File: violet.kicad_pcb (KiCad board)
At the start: 2 copper layers, 190 x 204 mm, 47 parts, among them J1 NEIGHBOR1, J10 Conn_01x08, J2 NEIGHBOR2, J3 NEIGHBOR1, J4 BONUS_ROW, J5 NEIGHBOR2, J6 NEIGHBOR1, J7 BONUS_ROW, J8 BONUS_ROW, J9 NEIGHBOR2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

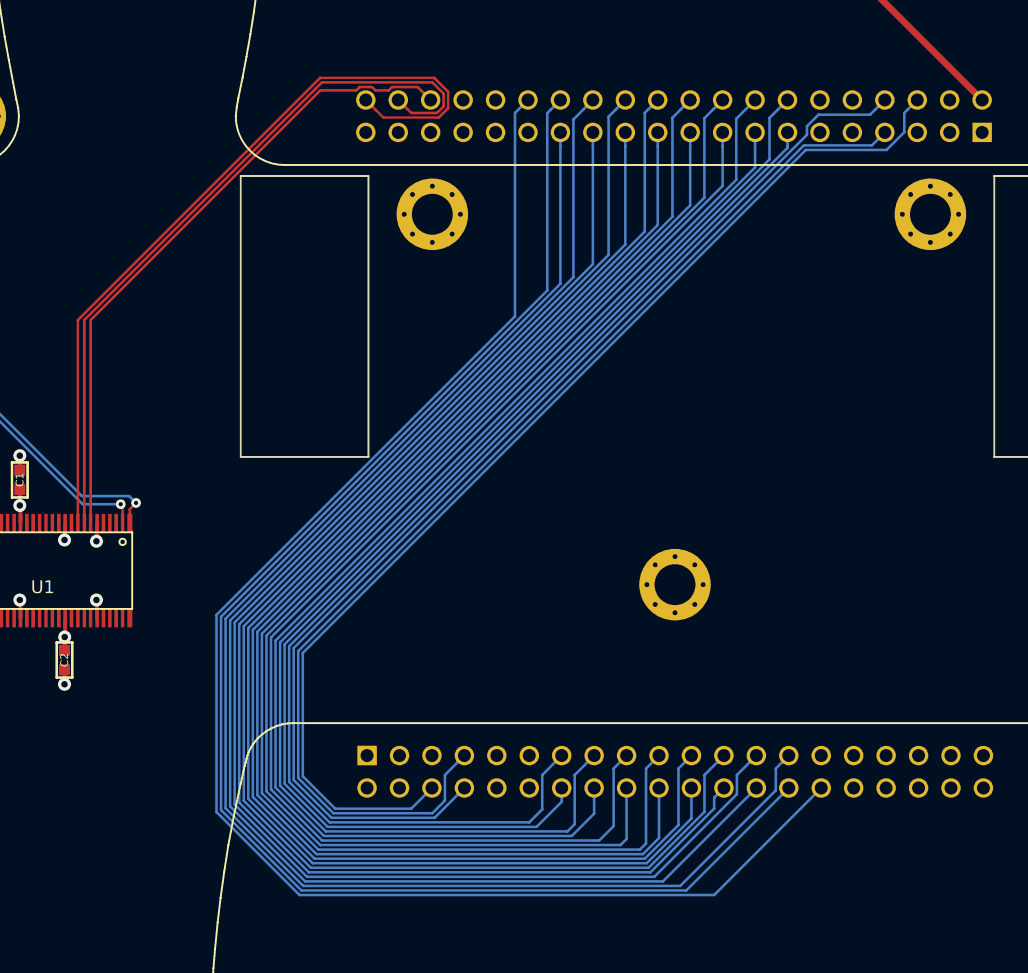
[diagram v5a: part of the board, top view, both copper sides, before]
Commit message: Re-map I/O expanders for easier routing
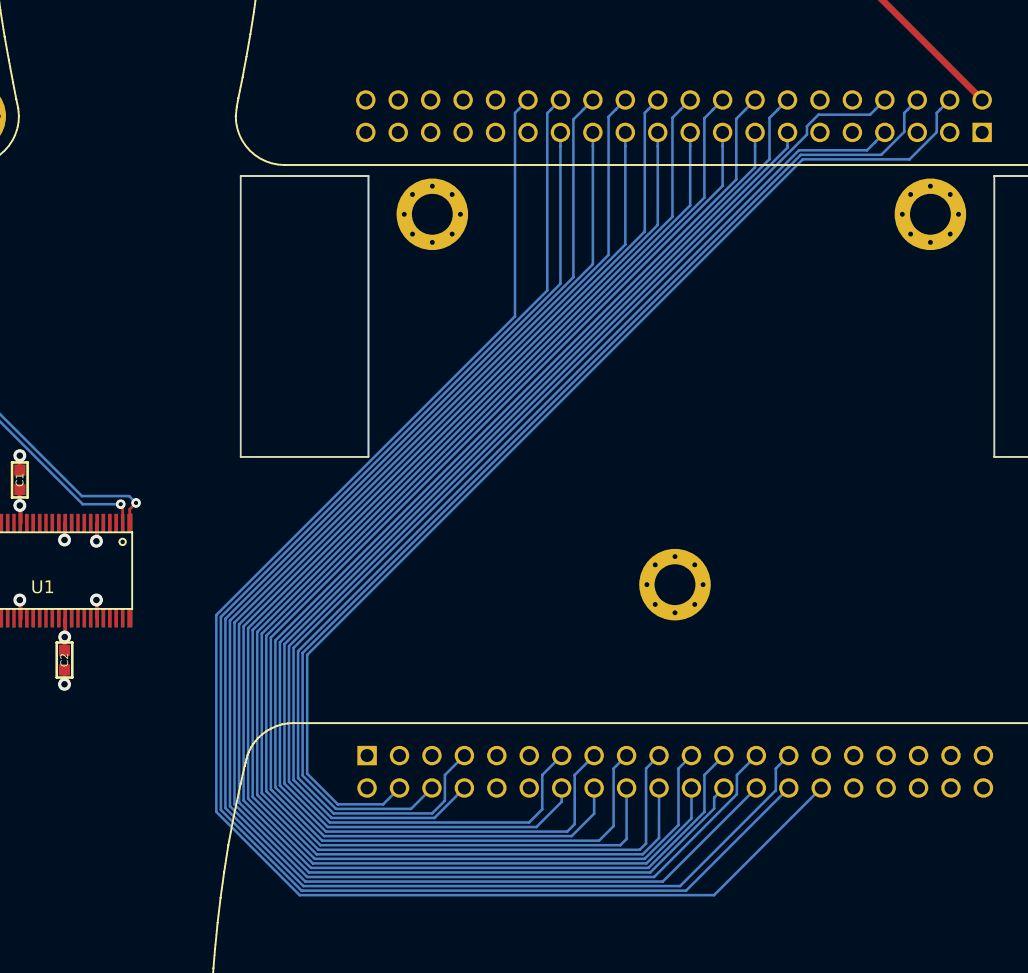
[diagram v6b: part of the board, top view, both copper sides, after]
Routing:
- net /EUT_P0_0: track 0.00 -> 87.2 mm
- net /U1_IO0_5: track 61.8 -> 0.00 mm
- net /U1_IO0_4: track 57.2 -> 0.00 mm
- net /U1_IO0_3: track 50.7 -> 0.00 mm

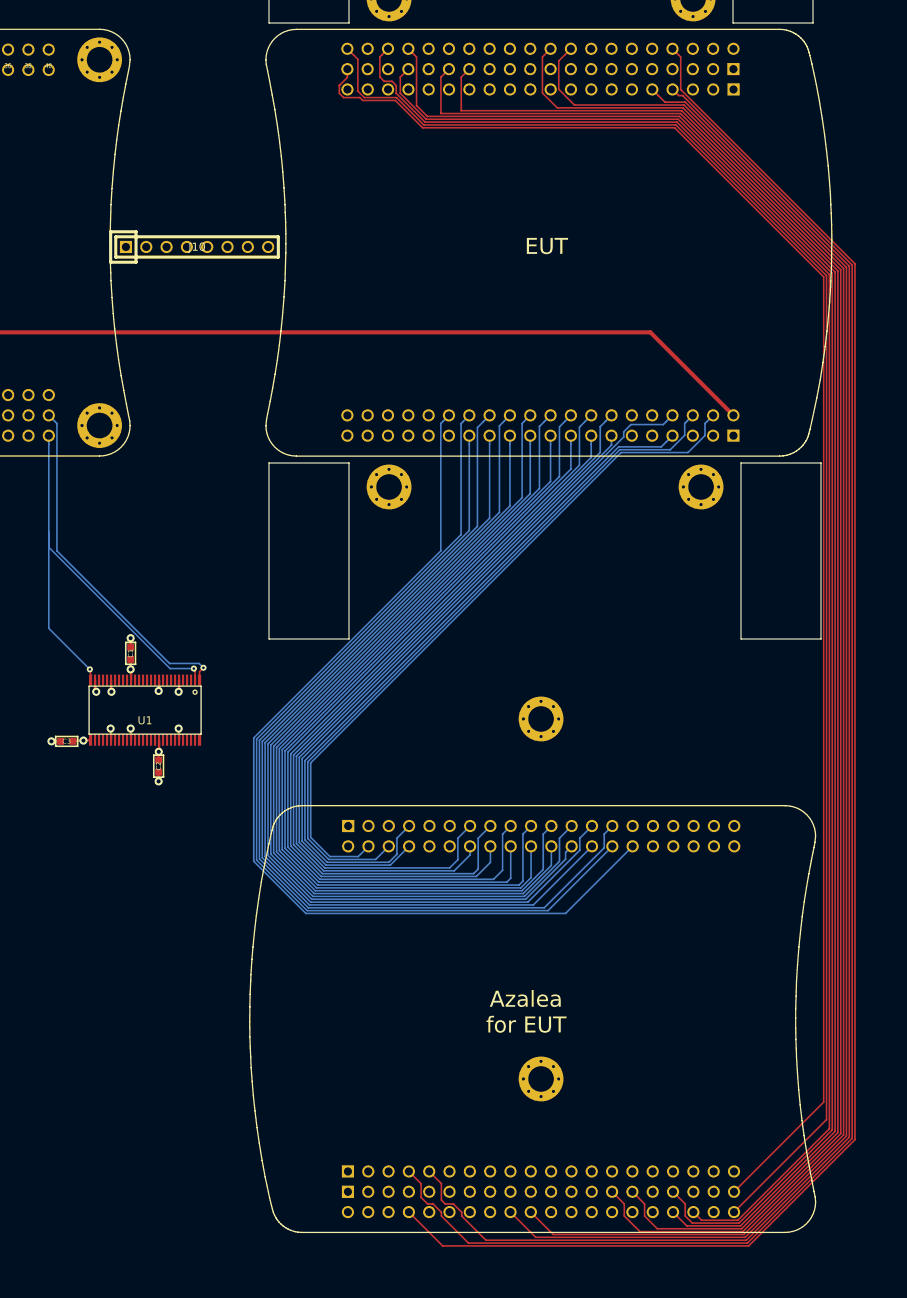
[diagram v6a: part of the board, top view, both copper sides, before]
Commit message: Route most of U1
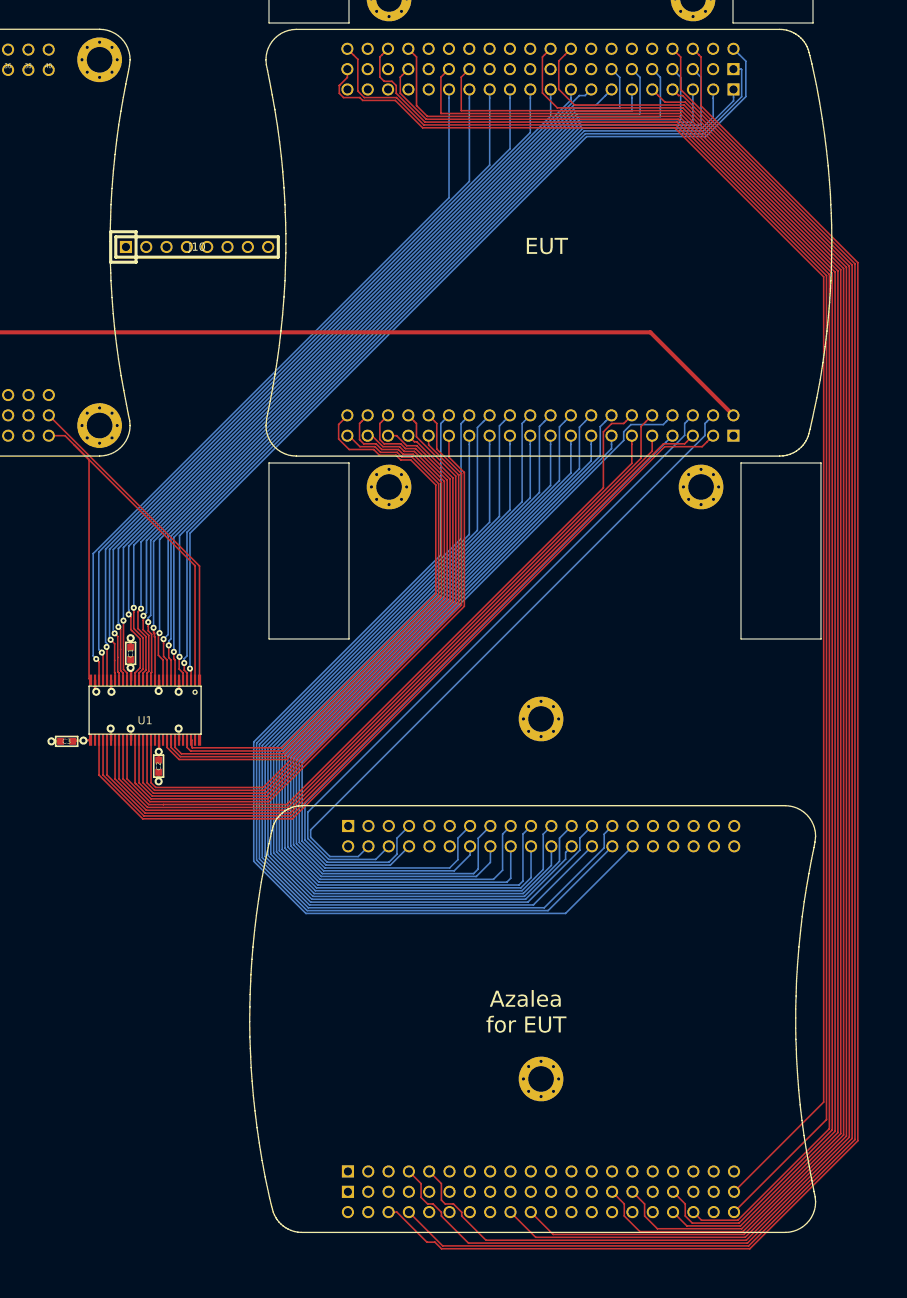
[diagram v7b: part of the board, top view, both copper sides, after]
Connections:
- J3 pad 10: /U1_IO4_3 -> /U1_IO2_7
- J3 pad 11: /U2_IO0_2 -> /U1_IO3_0
- J3 pad 12: /U1_IO4_2 -> /U1_IO3_1
- J3 pad 29: /U1_IO2_1 -> /U1_IO3_2
- J3 pad 3: /U1_IO4_7 -> /U1_IO2_4
- J3 pad 31: /U1_IO1_7 -> /U1_IO3_4
- J3 pad 32: /U1_IO1_6 -> /U1_IO3_3
- J3 pad 33: /U1_IO1_5 -> /U1_IO3_6
- J3 pad 34: /U1_IO1_4 -> /U1_IO3_5
- J3 pad 35: /U1_IO1_3 -> /U1_IO3_7
- J3 pad 36: /U1_IO0_3 -> /U1_IO4_2
- J3 pad 37: /U1_IO2_2 -> /U1_IO4_3
- J3 pad 38: /U1_IO0_4 -> /U1_IO4_4
- J3 pad 39: /U1_IO2_0 -> /U1_IO4_6
- J3 pad 40: /U1_IO0_5 -> /U1_IO4_7
- J3 pad 5: /U1_IO4_6 -> /U1_IO2_5
- J3 pad 9: /U1_IO4_4 -> /U1_IO2_6
- J4 pad 1: /U1_IO0_1 -> /U1_IO0_2
- J4 pad 10: /U2_IO1_6 -> /U1_IO1_6
- J4 pad 11: /U1_IO2_3 -> /U1_IO1_7
- J4 pad 12: /U2_IO1_5 -> /U1_IO2_0
- J4 pad 13: /U2_IO1_4 -> /U1_IO2_1
- J4 pad 14: /U2_IO1_3 -> /U1_IO2_2
- J4 pad 15: /U2_IO1_2 -> /U1_IO2_3
- J4 pad 16: /U2_IO1_1 -> /U1_IO4_6
- J4 pad 17: /U2_IO1_0 -> /U1_IO4_7
- J4 pad 18: /U2_IO0_7 -> /U2_IO2_2
- J4 pad 19: /U2_IO0_6 -> /U2_IO1_7
- J4 pad 2: /U1_IO0_0 -> /U1_IO0_3
- J4 pad 20: /U2_IO0_5 -> /U2_IO1_6
- J4 pad 3: /U2_IO2_3 -> /U1_IO0_5
- J4 pad 6: /U2_IO2_2 -> /U1_IO1_1
- J4 pad 7: /U2_IO2_1 -> /U1_IO1_3
- J4 pad 8: /U2_IO2_0 -> /U1_IO1_4
- J4 pad 9: /U2_IO1_7 -> /U1_IO1_5
- J5 pad 1: /U2_IO2_4 -> /U1_IO0_1
- J5 pad 10: /U2_IO3_2 -> /U2_IO2_5
- J5 pad 11: /U1_IO0_7 -> /U1_IO1_0
- J5 pad 12: /U1_IO1_2 -> /U2_IO2_6
- J5 pad 13: /U2_IO3_5 -> /U1_IO1_2
- J5 pad 14: /U2_IO3_4 -> /U2_IO2_7
- J5 pad 15: /U2_IO3_7 -> /U2_IO3_1
- J5 pad 16: /U2_IO3_6 -> /U1_IO3_0
- J5 pad 17: /U2_IO4_1 -> /U2_IO3_2
- J5 pad 19: /U2_IO4_3 -> /U2_IO3_3
- J5 pad 2: /U1_IO2_4 -> /U1_IO0_0
- J5 pad 21: /U1_IO1_0 -> /U2_IO3_5
- J5 pad 22: /U2_IO0_1 -> /U2_IO3_4
- J5 pad 23: /U2_IO4_4 -> /U2_IO3_7
- J5 pad 24: /U2_IO0_2 -> /U2_IO3_6
- J5 pad 25: /U2_IO4_5 -> /U2_IO4_1
- J5 pad 26: /U2_IO0_3 -> /U1_IO4_0
- J5 pad 28: /U2_IO2_7 -> /U1_IO4_2
- J5 pad 3: /U2_IO2_6 -> /U1_IO0_2
- J5 pad 30: /U1_IO2_7 -> /U2_IO4_3
- J5 pad 31: /U2_IO0_0 -> /U2_IO4_5
- J5 pad 32: /U1_IO2_6 -> /U2_IO4_4
- J5 pad 35: /U2_IO0_4 -> /U2_IO2_3
- J5 pad 37: /U1_IO1_1 -> /U2_IO2_0
- J5 pad 38: /U1_IO2_5 -> /U2_IO2_1
- J5 pad 4: /U2_IO2_5 -> /U2_IO2_4
- J5 pad 5: /U1_IO0_6 -> /U1_IO0_4
- J5 pad 7: /U2_IO3_1 -> /U1_IO0_6
- J5 pad 9: /U2_IO3_3 -> /U1_IO0_7
- U1 pad 36: Net-(U1-Pad36) -> /U1_IO3_0
- U1 pad 37: Net-(U1-Pad37) -> /U1_IO3_1
- U1 pad 38: Net-(U1-Pad38) -> /U1_IO3_2
- U1 pad 40: Net-(U1-Pad40) -> /U1_IO3_3
- U1 pad 41: Net-(U1-Pad41) -> /U1_IO3_4
- U1 pad 42: Net-(U1-Pad42) -> /U1_IO3_5
- U1 pad 43: Net-(U1-Pad43) -> /U1_IO3_6
- U1 pad 44: Net-(U1-Pad44) -> /U1_IO3_7
- U1 pad 5: Net-(U1-Pad5) -> /U1_IO0_2
- U2 pad 10: /U2_IO0_6 -> Net-(U2-Pad10)
- U2 pad 12: /U2_IO0_7 -> Net-(U2-Pad12)
- U2 pad 13: /U2_IO1_0 -> Net-(U2-Pad13)
- U2 pad 14: /U2_IO1_1 -> Net-(U2-Pad14)
- U2 pad 15: /U2_IO1_2 -> Net-(U2-Pad15)
- U2 pad 16: /U2_IO1_3 -> Net-(U2-Pad16)
- U2 pad 17: /U2_IO1_4 -> Net-(U2-Pad17)
- U2 pad 19: /U2_IO1_5 -> Net-(U2-Pad19)
- U2 pad 3: /U2_IO0_0 -> Net-(U2-Pad3)
- U2 pad 36: Net-(U2-Pad36) -> /U1_IO3_0
- U2 pad 4: /U2_IO0_1 -> Net-(U2-Pad4)
- U2 pad 45: Net-(U2-Pad45) -> /U1_IO4_0
- U2 pad 48: Net-(U2-Pad48) -> /U1_IO4_2
- U2 pad 5: /U2_IO0_2 -> Net-(U2-Pad5)
- U2 pad 53: Net-(U2-Pad53) -> /U1_IO4_6
- U2 pad 54: Net-(U2-Pad54) -> /U1_IO4_7
- U2 pad 7: /U2_IO0_3 -> Net-(U2-Pad7)
- U2 pad 8: /U2_IO0_4 -> Net-(U2-Pad8)
- U2 pad 9: /U2_IO0_5 -> Net-(U2-Pad9)
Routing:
- net /EUT_ADCCLK: track 0.00 -> 211.2 mm
- net /U1_IO0_0: track 0.00 -> 117.1 mm, vias 0 -> 1
- net /U1_IO0_1: track 0.00 -> 115.1 mm, vias 0 -> 1
- net /U1_IO0_4: track 0.00 -> 113.2 mm, vias 0 -> 1
- net /U1_IO0_6: track 0.00 -> 111.5 mm, vias 0 -> 1
- net /U1_IO0_2: track 0.00 -> 111.5 mm, vias 0 -> 1
- net /U1_IO0_3: track 0.00 -> 110.6 mm, vias 0 -> 1
- net /U1_IO0_5: track 0.00 -> 109.6 mm, vias 0 -> 1
- net /U1_IO0_7: track 0.00 -> 109.1 mm, vias 0 -> 1
- net /U1_IO1_0: track 0.00 -> 107.1 mm, vias 0 -> 1
- net /U1_IO1_2: track 0.00 -> 105.6 mm, vias 0 -> 1
- net /U1_IO1_1: track 0.00 -> 103.6 mm, vias 0 -> 1
- net /U1_IO2_4: track 0.00 -> 103.2 mm
- net /U1_IO1_3: track 0.00 -> 100.9 mm, vias 0 -> 1
- net /U1_IO2_5: track 0.00 -> 99.9 mm
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
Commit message: Complete routing of PCB; update routing in schematic for ease of routing on PCB
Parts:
- added C9: 100nF, gsg-modules:0603, F.Cu at (148.1, 57.8)
- moved R1 172.0 mm to (137.3, 165.8)
- moved R3 165.3 mm to (130.4, 165.8)
- moved R2 165.2 mm to (133.8, 165.8)
- moved C6 69.9 mm to (144.1, 69.7), turned to 270 degrees
- moved C5 66.4 mm to (139.6, 69.2), turned to 270 degrees
- moved R4 62.0 mm to (117.5, 61.5)
- moved R6 61.4 mm to (125.8, 61.5)
- moved R5 59.8 mm to (121.7, 61.5)
- moved C4 52.2 mm to (136.2, 54.0), turned to 90 degrees
- moved J1 42.2 mm to (111.3, 85.7)
- moved J2 42.2 mm to (111.3, 131.4)
- moved J3 42.2 mm to (196.9, 131.4)
- moved J8 42.2 mm to (196.9, 224.6)
- moved MH10 42.2 mm to (66.0, 238.1)
- moved MH15 42.2 mm to (112.0, 168.1)
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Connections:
- J4 pad 16: /U1_IO4_6 -> /U2_IO2_4
- J4 pad 17: /U1_IO4_7 -> /U2_IO2_3
- J4 pad 18: /U2_IO2_2 -> /U2_IO2_1
- J4 pad 19: /U2_IO1_7 -> /U2_IO1_6
- J4 pad 20: /U2_IO1_6 -> /U2_IO1_5
- J5 pad 10: /U2_IO2_5 -> /U2_IO4_5
- J5 pad 12: /U2_IO2_6 -> /U2_IO4_4
- J5 pad 14: /U2_IO2_7 -> /U2_IO4_3
- J5 pad 15: /U2_IO3_1 -> /U2_IO4_1
- J5 pad 16: /U1_IO3_0 -> /U2_IO4_2
- J5 pad 17: /U2_IO3_2 -> /U2_IO4_0
- J5 pad 19: /U2_IO3_3 -> /U2_IO3_7
- J5 pad 22: /U2_IO3_4 -> /U2_IO3_6
- J5 pad 23: /U2_IO3_7 -> /U2_IO3_3
- J5 pad 24: /U2_IO3_6 -> /U2_IO3_4
- J5 pad 25: /U2_IO4_1 -> /U2_IO3_1
- J5 pad 26: /U1_IO4_0 -> /U2_IO3_2
- J5 pad 28: /U1_IO4_2 -> /U2_IO3_0
- J5 pad 3: /U1_IO0_2 -> /U2_IO4_6
- J5 pad 30: /U2_IO4_3 -> /U2_IO2_7
- J5 pad 31: /U2_IO4_5 -> /U2_IO2_5
- J5 pad 32: /U2_IO4_4 -> /U2_IO2_6
- J5 pad 35: /U2_IO2_3 -> /U2_IO2_2
- J5 pad 37: /U2_IO2_0 -> /U2_IO1_7
- J5 pad 38: /U2_IO2_1 -> /U2_IO2_0
- J5 pad 4: /U2_IO2_4 -> /U2_IO4_7
- U2 pad 19: Net-(U2-Pad19) -> /U2_IO1_5
- U2 pad 36: /U1_IO3_0 -> /U2_IO3_0
- U2 pad 45: /U1_IO4_0 -> /U2_IO4_0
- U2 pad 48: /U1_IO4_2 -> /U2_IO4_2
- U2 pad 53: /U1_IO4_6 -> /U2_IO4_6
- U2 pad 54: /U1_IO4_7 -> /U2_IO4_7
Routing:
- net /U2_IO4_6: track 0.00 -> 113.4 mm
- net /U2_IO4_7: track 0.00 -> 112.0 mm
- net /P9_5: track 0.00 -> 107.2 mm, vias 0 -> 1
- net /U2_IO4_5: track 0.00 -> 106.3 mm
- net /U2_IO4_4: track 0.00 -> 104.4 mm
- net /U2_IO4_3: track 0.00 -> 102.4 mm
- net /U2_IO4_1: track 0.00 -> 102.0 mm
- net /P9_6: track 0.00 -> 101.9 mm, vias 0 -> 1
- net /U2_IO4_2: track 0.00 -> 100.4 mm
- net /U2_IO4_0: track 0.00 -> 97.7 mm
- net /U2_IO3_7: track 0.00 -> 95.6 mm
- net /P1_17: track 0.00 -> 94.4 mm, vias 0 -> 1
- net /I2C0_SCL: track 69.6 -> 163.5 mm, vias 0 -> 2
- net /U2_IO3_5: track 0.00 -> 91.5 mm
- net /U2_IO3_6: track 0.00 -> 90.0 mm
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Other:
- outline, holes or cut-outs redrawn
